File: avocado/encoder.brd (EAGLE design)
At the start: 23.5 x 26 mm, 4 parts, among them U2 AS5048A-HTSP-500

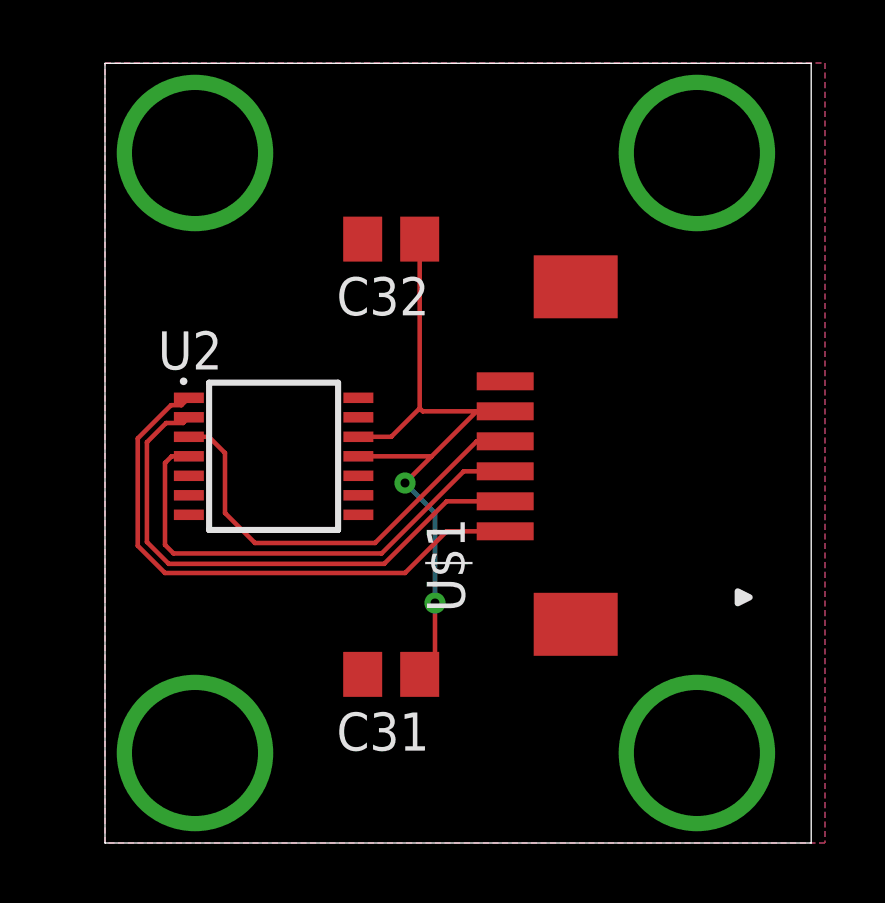
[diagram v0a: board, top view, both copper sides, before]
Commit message: fixed all airwires, still need to fix DRC
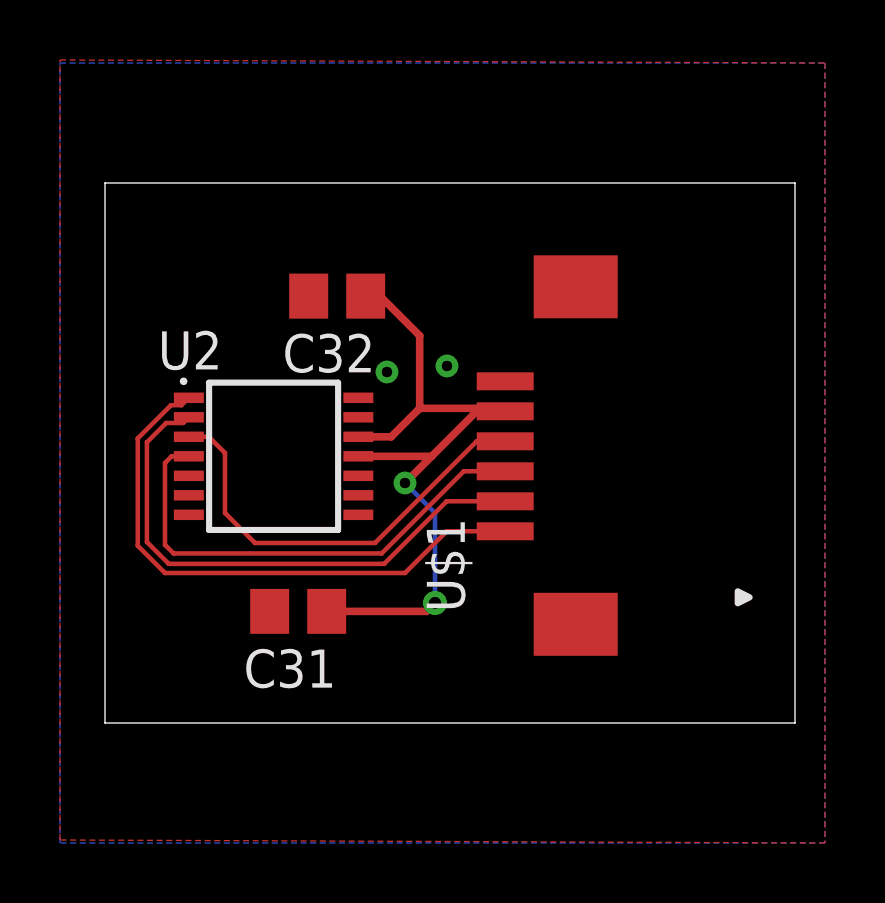
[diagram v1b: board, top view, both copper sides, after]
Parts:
- moved C31 3.74 mm to (6.44, 7.72)
- moved C32 2.62 mm to (7.74, 18.2)
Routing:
- net ENC_PWR: track 25.3 -> 24.8 mm
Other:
- board size 23.5 x 26 mm -> 23 x 18 mm
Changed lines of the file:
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@@
 <setting verticaltext="up"/>
 </settings>
-<grid distance="1" unitdist="mm" unit="mm" style="lines" multiple="1" display="no" altdistance="5" altunitdist="mil" altunit="mil"/>
+<grid distance="3.93700787" unitdist="mil" unit="mil" style="lines" multiple="1" display="no" altdistance="5" altunitdist="mil" altunit="mil"/>
 <layers>
 <layer number="1" name="Top" color="4" fill="1" visible="yes" active="yes"/>
@@
 <board>
 <plain>
-<wire x1="0" y1="0" x2="23.54" y2="0" width="0" layer="20"/>
-<wire x1="23.54" y1="0" x2="23.54" y2="25.99" width="0" layer="20"/>
-<wire x1="23.54" y1="25.99" x2="0" y2="25.99" width="0" layer="20"/>
-<wire x1="0" y1="25.99" x2="0" y2="0" width="0" layer="20"/>
+<wire x1="0" y1="4" x2="23" y2="4" width="0" layer="20"/>
+<wire x1="23" y1="4" x2="23" y2="22" width="0" layer="20"/>
+<wire x1="23" y1="22" x2="0" y2="22" width="0" layer="20"/>
+<wire x1="0" y1="22" x2="0" y2="4" width="0" layer="20"/>
 </plain>
 <attributes>
@@
 </autorouter>
 <elements>
-<element name="C31" library="rcl" library_urn="urn:adsk.eagle:library:334" package="C0805" package3d_urn="urn:adsk.eagle:package:23617/2" value="1uF" x="9.54" y="5.62" rot="R180">
-<attribute name="SPICEPREFIX" value="C" x="9.54" y="5.62" size="1.778" layer="27" rot="R180" display="off"/>
+<element name="C31" library="rcl" library_urn="urn:adsk.eagle:library:334" package="C0805" package3d_urn="urn:adsk.eagle:package:23617/2" value="1uF" x="6.44" y="7.72" rot="R180">
+<attribute name="SPICEPREFIX" value="C" x="6.44" y="7.72" size="1.778" layer="27" rot="R180" display="off"/>
 </element>
-<element name="C32" library="rcl" library_urn="urn:adsk.eagle:library:334" package="C0805" package3d_urn="urn:adsk.eagle:package:23617/2" value="1uF" x="9.54" y="20.13" rot="R180">
-<attribute name="SPICEPREFIX" value="C" x="9.54" y="20.13" size="1.778" layer="27" rot="R180" display="off"/>
+<element name="C32" library="rcl" library_urn="urn:adsk.eagle:library:334" package="C0805" package3d_urn="urn:adsk.eagle:package:23617/2" value="1uF" x="7.74" y="18.23" rot="R180">
+<attribute name="SPICEPREFIX" value="C" x="7.74" y="18.23" size="1.778" layer="27" rot="R180" display="off"/>
 </element>
 <element name="U$1" library="avocado" package="1MM-FPC-6PIN" value="0522070633" x="16.59" y="12.89" rot="R90"/>
@@
 <contactref element="U$1" pad="6"/>
 <polygon width="0.1524" layer="1">
-<vertex x="0" y="26"/>
+<vertex x="-1.5" y="26.1"/>
 <vertex x="24" y="26"/>
 <vertex x="24" y="0"/>
-<vertex x="0" y="0"/>
+<vertex x="-1.5" y="0.1"/>
 </polygon>
 <polygon width="0.1524" layer="16">
-<vertex x="0" y="26"/>
+<vertex x="-1.5" y="26"/>
 <vertex x="24" y="26"/>
 <vertex x="24" y="0"/>
-<vertex x="0" y="0"/>
+<vertex x="-1.5" y="0"/>
 </polygon>
-<via x="3" y="3" extent="1-16" drill="4.2"/>
-<via x="3" y="23" extent="1-16" drill="4.2"/>
-<via x="19.73" y="23" extent="1-16" drill="4.2"/>
-<via x="19.73" y="3" extent="1-16" drill="4.2"/>
+<via x="9.4" y="15.7" extent="1-16" drill="0.35"/>
+<via x="11.4" y="15.9" extent="1-16" drill="0.35"/>
 </signal>
 <signal name="ENC_SS">
@@
 <contactref element="C31" pad="1"/>
 <contactref element="U$1" pad="5"/>
-<wire x1="8.445" y1="12.89" x2="10.89" y2="12.89" width="0.1524" layer="1"/>
-<wire x1="12.39" y1="14.39" x2="13.34" y2="14.39" width="0.1524" layer="1"/>
-<wire x1="10.89" y1="12.89" x2="12.39" y2="14.39" width="0.1524" layer="1"/>
-<wire x1="10.89" y1="6.02" x2="10.49" y2="5.62" width="0.1524" layer="1"/>
-<wire x1="8.445" y1="13.54" x2="9.54" y2="13.54" width="0.1524" layer="1"/>
-<wire x1="10.49" y1="14.49" x2="10.49" y2="20.13" width="0.1524" layer="1"/>
-<wire x1="9.54" y1="13.54" x2="10.49" y2="14.49" width="0.1524" layer="1"/>
-<wire x1="13.34" y1="14.39" x2="10.59" y2="14.39" width="0.1524" layer="1"/>
-<wire x1="10.59" y1="14.39" x2="10.49" y2="14.49" width="0.1524" layer="1"/>
-<wire x1="10.49" y1="5.62" x2="11" y2="6.13" width="0.1524" layer="1"/>
-<wire x1="11" y1="6.13" x2="11" y2="8" width="0.1524" layer="1"/>
-<via x="11" y="8" extent="1-16" drill="0.3"/>
+<wire x1="8.445" y1="12.89" x2="10.89" y2="12.89" width="0.254" layer="1"/>
+<wire x1="12.39" y1="14.39" x2="13.1" y2="14.39" width="0.1524" layer="1"/>
+<wire x1="13.1" y1="14.39" x2="13.34" y2="14.39" width="0.1524" layer="1"/>
+<wire x1="10.89" y1="12.89" x2="12.39" y2="14.39" width="0.254" layer="1"/>
+<wire x1="8.445" y1="13.54" x2="9.54" y2="13.54" width="0.254" layer="1"/>
+<wire x1="10.49" y1="14.49" x2="9.54" y2="13.54" width="0.254" layer="1"/>
+<via x="11" y="8" extent="1-16" drill="0.4"/>
 <wire x1="11" y1="8" x2="11" y2="11" width="0.1524" layer="16"/>
 <wire x1="11" y1="11" x2="10" y2="12" width="0.1524" layer="16"/>
-<via x="10" y="12" extent="1-16" drill="0.3"/>
-<wire x1="10" y1="12" x2="10.89" y2="12.89" width="0.1524" layer="1"/>
+<via x="10" y="12" extent="1-16" drill="0.35"/>
+<wire x1="10" y1="12" x2="10.89" y2="12.89" width="0.254" layer="1"/>
+<wire x1="7.39" y1="7.72" x2="10.72" y2="7.72" width="0.254" layer="1"/>
+<wire x1="10.72" y1="7.72" x2="11" y2="8" width="0.254" layer="1"/>
+<wire x1="8.69" y1="18.23" x2="9.17" y2="18.23" width="0.1524" layer="1"/>
+<wire x1="10.49" y1="16.91" x2="10.49" y2="14.49" width="0.254" layer="1"/>
+<wire x1="9.17" y1="18.23" x2="10.49" y2="16.91" width="0.254" layer="1"/>
+<wire x1="10.49" y1="14.49" x2="13" y2="14.49" width="0.254" layer="1"/>
+<wire x1="13" y1="14.49" x2="13.1" y2="14.39" width="0.1524" layer="1"/>
 </signal>
 </signals>

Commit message: new gerber files and updated peripheral/main board
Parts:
- moved U$1 1.02 mm to (17.6, 12.9), flipped to the bottom
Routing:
- net ENC_SS: track 19.0 -> 26.6 mm, vias 0 -> 1
- net ENC_MOSI: track 16.2 -> 23.7 mm, vias 0 -> 1
- net ENC_MISO: track 14.6 -> 22.1 mm, vias 0 -> 1
- net ENC_CLK: track 18.2 -> 25.7 mm, vias 0 -> 1
- net ENC_PWR: track 24.8 -> 23.7 mm
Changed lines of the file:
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@@
 <attribute name="SPICEPREFIX" value="C" x="7.74" y="18.23" size="1.778" layer="27" rot="R180" display="off"/>
 </element>
-<element name="U$1" library="avocado" package="1MM-FPC-6PIN" value="0522070633" x="16.59" y="12.89" rot="R90"/>
+<element name="U$1" library="avocado" package="1MM-FPC-6PIN" value="0522070633" x="17.61" y="12.89" rot="MR90"/>
 <element name="U2" library="avocado" package="SOP65P640X120-14N" value="AS5048A-HTSP-500" x="5.62" y="12.89">
 <attribute name="AVAILABILITY" value="Unavailable" x="5.62" y="12.89" size="1.778" layer="27" display="off"/>
@@
 <wire x1="1.0922" y1="13.4854875" x2="2.2003125" y2="14.5936" width="0.1524" layer="1"/>
 <wire x1="2" y1="9" x2="10" y2="9" width="0.1524" layer="1"/>
-<wire x1="11.39" y1="10.39" x2="13.34" y2="10.39" width="0.1524" layer="1"/>
+<wire x1="11.39" y1="10.39" x2="20.86" y2="10.39" width="0.1524" layer="16"/>
 <wire x1="10" y1="9" x2="11.39" y2="10.39" width="0.1524" layer="1"/>
+<via x="11.39" y="10.39" extent="1-16" drill="0.35"/>
 </signal>
 <signal name="ENC_CLK">
 <contactref element="U2" pad="2"/>
 <contactref element="U$1" pad="2"/>
-<wire x1="13.34" y1="11.39" x2="11.39" y2="11.39" width="0.1524" layer="1"/>
+<wire x1="20.86" y1="11.39" x2="11.39" y2="11.39" width="0.1524" layer="16"/>
 <wire x1="9.3048" y1="9.3048" x2="11.39" y2="11.39" width="0.1524" layer="1"/>
 <wire x1="2.795" y1="14.19" x2="2.605" y2="14" width="0.1524" layer="1"/>
@@
 <wire x1="1.397" y1="10.03405625" x2="2.12625625" y2="9.3048" width="0.1524" layer="1"/>
 <wire x1="2.12625625" y1="9.3048" x2="9.3048" y2="9.3048" width="0.1524" layer="1"/>
+<via x="11.39" y="11.39" extent="1-16" drill="0.35"/>
 </signal>
 <signal name="ENC_MOSI">
@@
 <wire x1="2.286" y1="9.652" x2="2" y2="9.938" width="0.1524" layer="1"/>
 <wire x1="2" y1="9.938" x2="2" y2="12.668" width="0.1524" layer="1"/>
-<wire x1="11.95894375" y1="12.39" x2="13.34" y2="12.39" width="0.1524" layer="1"/>
+<wire x1="11.95894375" y1="12.39" x2="20.86" y2="12.39" width="0.1524" layer="16"/>
 <wire x1="9.22094375" y1="9.652" x2="11.95894375" y2="12.39" width="0.1524" layer="1"/>
+<via x="11.95894375" y="12.39" extent="1-16" drill="0.35"/>
 </signal>
 <signal name="ENC_MISO">
 <contactref element="U2" pad="3"/>
 <contactref element="U$1" pad="4"/>
-<wire x1="13.34" y1="13.39" x2="12.39" y2="13.39" width="0.1524" layer="1"/>
+<wire x1="20.86" y1="13.39" x2="12.39" y2="13.39" width="0.1524" layer="16"/>
 <wire x1="9" y1="10" x2="5" y2="10" width="0.1524" layer="1"/>
 <wire x1="5" y1="10" x2="4" y2="11" width="0.1524" layer="1"/>
@@
 <wire x1="3.46" y1="13.54" x2="2.795" y2="13.54" width="0.1524" layer="1"/>
 <wire x1="12.39" y1="13.39" x2="9" y2="10" width="0.1524" layer="1"/>
+<via x="12.39" y="13.39" extent="1-16" drill="0.35"/>
 </signal>
 <signal name="ENC_PWR">
@@
 <contactref element="U$1" pad="5"/>
 <wire x1="8.445" y1="12.89" x2="10.89" y2="12.89" width="0.254" layer="1"/>
-<wire x1="12.39" y1="14.39" x2="13.1" y2="14.39" width="0.1524" layer="1"/>
-<wire x1="13.1" y1="14.39" x2="13.34" y2="14.39" width="0.1524" layer="1"/>
+<wire x1="12.39" y1="14.39" x2="13.1" y2="14.39" width="0" layer="19" extent="1-16"/>
 <wire x1="10.89" y1="12.89" x2="12.39" y2="14.39" width="0.254" layer="1"/>
 <wire x1="8.445" y1="13.54" x2="9.54" y2="13.54" width="0.254" layer="1"/>
@@
 <wire x1="9.17" y1="18.23" x2="10.49" y2="16.91" width="0.254" layer="1"/>
 <wire x1="10.49" y1="14.49" x2="13" y2="14.49" width="0.254" layer="1"/>
-<wire x1="13" y1="14.49" x2="13.1" y2="14.39" width="0.1524" layer="1"/>
+<wire x1="13.1" y1="14.39" x2="20.86" y2="14.39" width="0" layer="19" extent="1-16"/>
+<wire x1="13" y1="14.49" x2="13.1" y2="14.39" width="0" layer="19" extent="1-1"/>
 </signal>
 </signals>

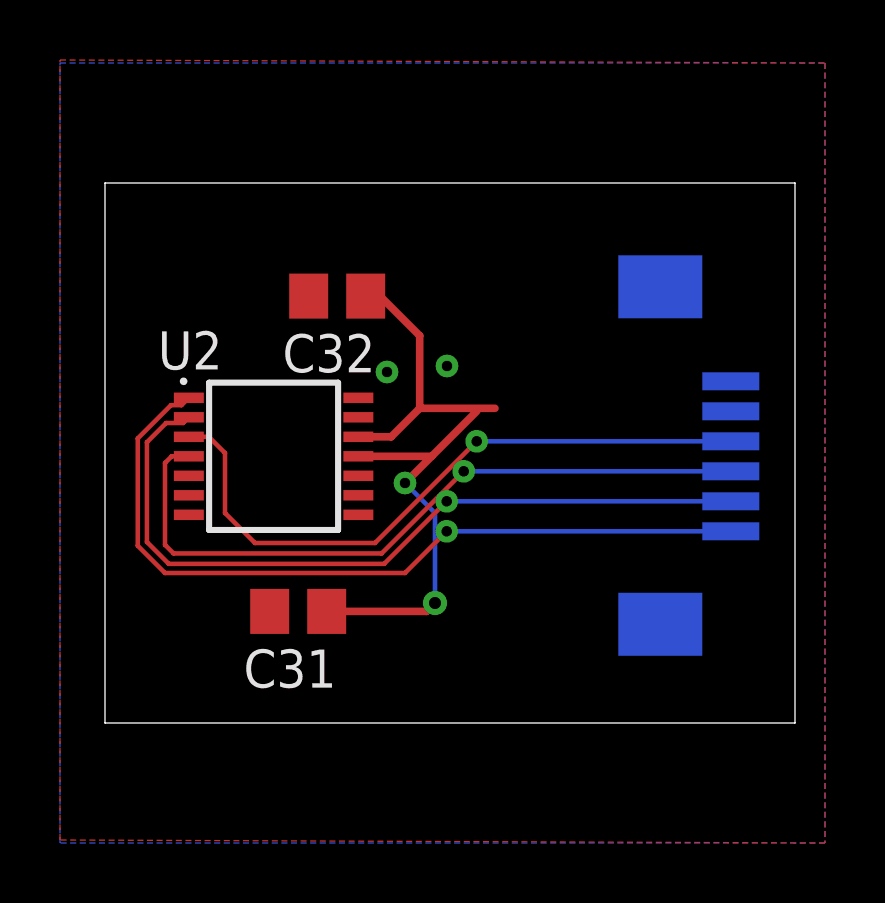
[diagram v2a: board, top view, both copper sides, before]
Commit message: updated encoder board size
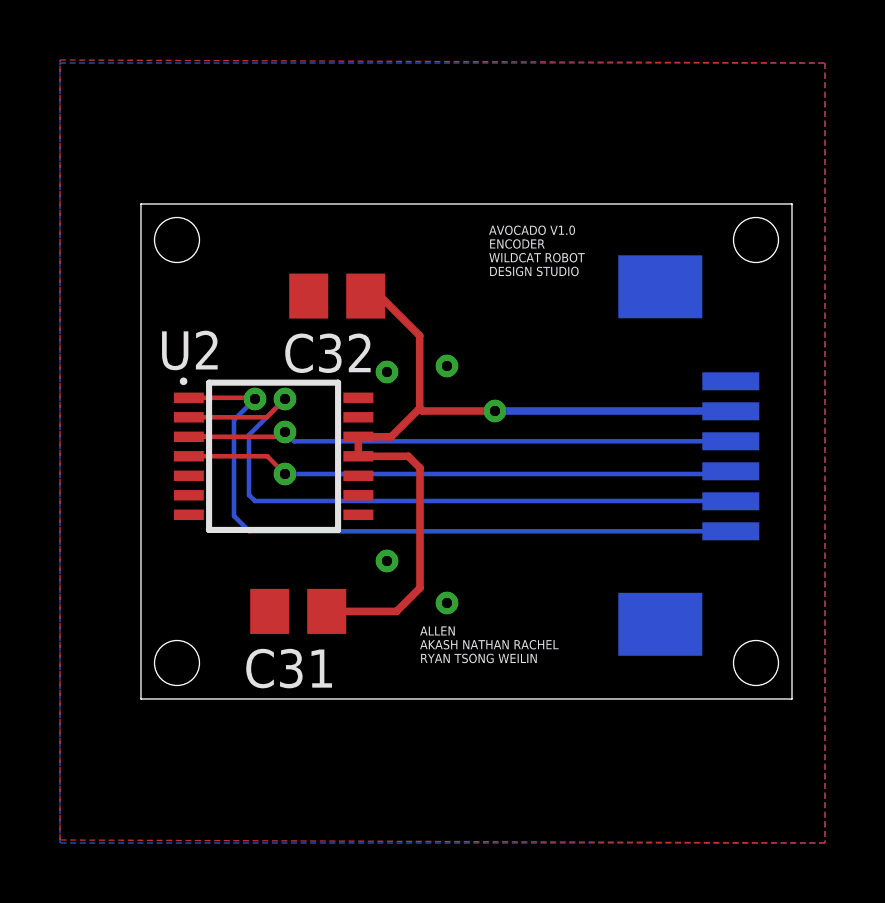
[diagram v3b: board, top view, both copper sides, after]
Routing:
- net ENC_MOSI: track 23.7 -> 18.3 mm
- net ENC_PWR: track 23.7 -> 27.9 mm, vias 2 -> 1
- net ENC_SS: track 26.6 -> 23.2 mm
- net ENC_MISO: track 22.1 -> 18.9 mm
- net ENC_CLK: track 25.7 -> 23.3 mm
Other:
- board size 23 x 18 mm -> 21.7 x 16.5 mm
- board text added: "ALLEN AKASH NATHAN RACHEL RYAN TSONG WEILIN"
- board text added: "AVOCADO V1.0 ENCODER WILDCAT ROBOT DESIGN STUDIO"
